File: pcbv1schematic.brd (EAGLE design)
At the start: 275.6 x 183.8 mm, 24 parts, among them IC1 L298, IC2 7805T

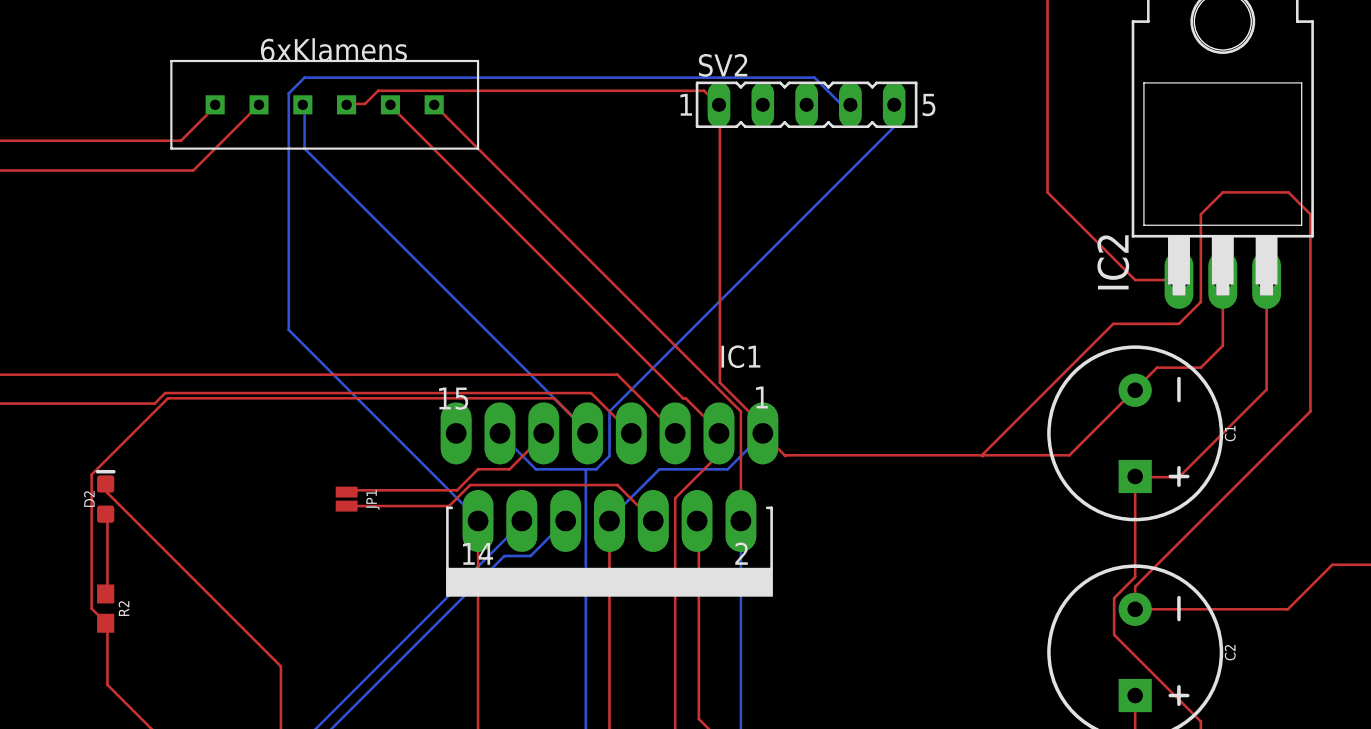
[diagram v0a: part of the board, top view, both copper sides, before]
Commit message: Fixes Label Name
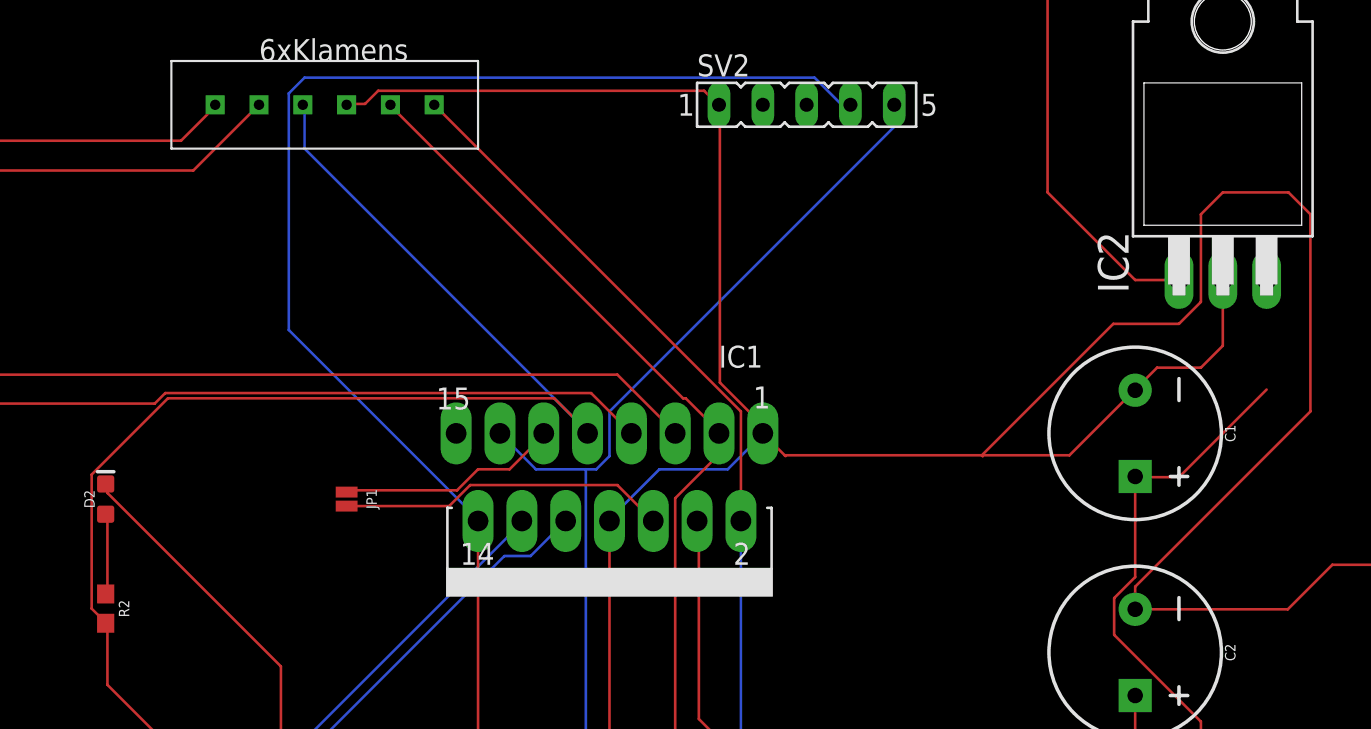
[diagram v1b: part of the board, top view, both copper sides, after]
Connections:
- net N$5 renamed 5V
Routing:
- net 5V: track 211.8 -> 205.0 mm
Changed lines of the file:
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@@
 <drawing>
 <settings>
-<setting alwaysvectorfont="yes"/>
+<setting alwaysvectorfont="no"/>
 <setting verticaltext="up"/>
 </settings>
@@
 <wire x1="43.1292" y1="39.3192" x2="43.18" y2="39.37" width="0.1524" layer="1"/>
 </signal>
-<signal name="N$5">
-<wire x1="125.73" y1="60.96" x2="128.27" y2="60.96" width="0.1524" layer="1"/>
-<wire x1="128.27" y1="60.96" x2="133.35" y2="66.04" width="0.1524" layer="1"/>
-<contactref element="IC2" pad="3"/>
-<contactref element="R2" pad="2"/>
-<contactref element="C1" pad="+"/>
-<contactref element="IC1" pad="9"/>
-<contactref element="U$3" pad="P$3"/>
-<contactref element="U$4" pad="P$3"/>
-<wire x1="125.73" y1="61.1124" x2="125.73" y2="61" width="0.1524" layer="16"/>
-<wire x1="65.2272" y1="53.34" x2="65.9892" y2="52.578" width="0.1524" layer="1"/>
-<wire x1="65.2272" y1="61.1124" x2="65.2272" y2="53.34" width="0.1524" layer="1"/>
-<wire x1="69.6468" y1="65.532" x2="65.2272" y2="61.1124" width="0.1524" layer="1"/>
-<wire x1="92.0496" y1="65.532" x2="69.6468" y2="65.532" width="0.1524" layer="1"/>
-<wire x1="94.0308" y1="63.5508" x2="92.0496" y2="65.532" width="0.1524" layer="1"/>
-<wire x1="65.9892" y1="52.578" x2="66.04" y2="52.49" width="0.1524" layer="1"/>
-<wire x1="94.0308" y1="63.5508" x2="93.98" y2="63.5" width="0.1524" layer="1"/>
-<wire x1="77.4192" y1="37.6428" x2="77.4192" y2="16.6116" width="0.1524" layer="1"/>
-<wire x1="66.1416" y1="48.9204" x2="77.4192" y2="37.6428" width="0.1524" layer="1"/>
-<wire x1="66.1416" y1="52.4256" x2="66.1416" y2="48.9204" width="0.1524" layer="1"/>
-<wire x1="77.4192" y1="16.6116" x2="77.47" y2="16.51" width="0.1524" layer="1"/>
-<wire x1="66.1416" y1="52.4256" x2="66.04" y2="52.49" width="0.1524" layer="1"/>
-<wire x1="77.5716" y1="80.01" x2="77.5716" y2="82.4484" width="0.1524" layer="16"/>
-<wire x1="94.0308" y1="63.5508" x2="77.5716" y2="80.01" width="0.1524" layer="16"/>
-<wire x1="77.5716" y1="82.4484" x2="77.47" y2="82.55" width="0.1524" layer="16"/>
-<wire x1="94.0308" y1="63.5508" x2="93.98" y2="63.5" width="0.1524" layer="16"/>
-<wire x1="125.73" y1="60.96" x2="125.73" y2="61" width="0.1524" layer="16"/>
-<wire x1="94.0308" y1="63.3984" x2="93.98" y2="63.5" width="0.1524" layer="1"/>
-<wire x1="133.35" y1="66.04" x2="133.35" y2="72.39" width="0.1524" layer="1"/>
-<wire x1="125.73" y1="55.1688" x2="125.73" y2="60.96" width="0.1524" layer="1"/>
-<wire x1="124.5108" y1="53.9496" x2="125.73" y2="55.1688" width="0.1524" layer="1"/>
-<wire x1="124.5108" y1="51.816" x2="124.5108" y2="53.9496" width="0.1524" layer="1"/>
-<wire x1="129.54" y1="46.7868" x2="124.5108" y2="51.816" width="0.1524" layer="1"/>
-<wire x1="129.54" y1="36.1188" x2="129.54" y2="46.7868" width="0.1524" layer="1"/>
-<wire x1="109.1184" y1="15.6972" x2="129.54" y2="36.1188" width="0.1524" layer="1"/>
-<wire x1="78.3336" y1="15.6972" x2="109.1184" y2="15.6972" width="0.1524" layer="1"/>
-<wire x1="77.5716" y1="16.4592" x2="78.3336" y2="15.6972" width="0.1524" layer="1"/>
-<wire x1="125.73" y1="60.96" x2="125.73" y2="61" width="0.1524" layer="1"/>
-<wire x1="77.5716" y1="16.4592" x2="77.47" y2="16.51" width="0.1524" layer="1"/>
-</signal>
 <signal name="N$7">
 <wire x1="116.84" y1="62.23" x2="124.46" y2="69.85" width="0.1524" layer="1"/>
@@
 <wire x1="137.16" y1="55.88" x2="143.51" y2="55.88" width="0.1524" layer="1"/>
 </signal>
+<signal name="5V">
+<contactref element="U$3" pad="P$3"/>
+<contactref element="IC2" pad="3"/>
+<contactref element="R2" pad="2"/>
+<contactref element="C1" pad="+"/>
+<wire x1="125.73" y1="61.1124" x2="125.73" y2="61" width="0.1524" layer="16"/>
+<wire x1="125.73" y1="60.96" x2="125.73" y2="61" width="0.1524" layer="16"/>
+<contactref element="IC1" pad="9"/>
+<wire x1="65.2272" y1="53.34" x2="65.9892" y2="52.578" width="0.1524" layer="1"/>
+<wire x1="65.2272" y1="61.1124" x2="65.2272" y2="53.34" width="0.1524" layer="1"/>
+<wire x1="69.6468" y1="65.532" x2="65.2272" y2="61.1124" width="0.1524" layer="1"/>
+<wire x1="92.0496" y1="65.532" x2="69.6468" y2="65.532" width="0.1524" layer="1"/>
+<wire x1="94.0308" y1="63.5508" x2="92.0496" y2="65.532" width="0.1524" layer="1"/>
+<wire x1="94.0308" y1="63.5508" x2="93.98" y2="63.5" width="0.1524" layer="1"/>
+<wire x1="77.5716" y1="80.01" x2="77.5716" y2="82.4484" width="0.1524" layer="16"/>
+<wire x1="94.0308" y1="63.5508" x2="77.5716" y2="80.01" width="0.1524" layer="16"/>
+<wire x1="94.0308" y1="63.5508" x2="93.98" y2="63.5" width="0.1524" layer="16"/>
+<wire x1="94.0308" y1="63.3984" x2="93.98" y2="63.5" width="0.1524" layer="1"/>
+<wire x1="125.73" y1="60.96" x2="128.27" y2="60.96" width="0.1524" layer="1"/>
+<wire x1="128.27" y1="60.96" x2="133.35" y2="66.04" width="0.1524" layer="1"/>
+<contactref element="U$4" pad="P$3"/>
+<wire x1="77.4192" y1="37.6428" x2="77.4192" y2="16.6116" width="0.1524" layer="1"/>
+<wire x1="66.1416" y1="48.9204" x2="77.4192" y2="37.6428" width="0.1524" layer="1"/>
+<wire x1="66.1416" y1="52.4256" x2="66.1416" y2="48.9204" width="0.1524" layer="1"/>
+<wire x1="77.4192" y1="16.6116" x2="77.47" y2="16.51" width="0.1524" layer="1"/>
+<wire x1="125.73" y1="55.1688" x2="125.73" y2="60.96" width="0.1524" layer="1"/>
+<wire x1="124.5108" y1="53.9496" x2="125.73" y2="55.1688" width="0.1524" layer="1"/>
+<wire x1="124.5108" y1="51.816" x2="124.5108" y2="53.9496" width="0.1524" layer="1"/>
+<wire x1="129.54" y1="46.7868" x2="124.5108" y2="51.816" width="0.1524" layer="1"/>
+<wire x1="129.54" y1="36.1188" x2="129.54" y2="46.7868" width="0.1524" layer="1"/>
+<wire x1="109.1184" y1="15.6972" x2="129.54" y2="36.1188" width="0.1524" layer="1"/>
+<wire x1="78.3336" y1="15.6972" x2="109.1184" y2="15.6972" width="0.1524" layer="1"/>
+<wire x1="77.5716" y1="16.4592" x2="78.3336" y2="15.6972" width="0.1524" layer="1"/>
+<wire x1="77.5716" y1="16.4592" x2="77.47" y2="16.51" width="0.1524" layer="1"/>
+<wire x1="133.35" y1="66.04" x2="133.35" y2="72.39" width="0" layer="19" extent="1-1"/>
+<wire x1="66.04" y1="52.49" x2="66.1416" y2="52.4256" width="0" layer="19" extent="1-1"/>
+<wire x1="65.9892" y1="52.578" x2="66.04" y2="52.49" width="0" layer="19" extent="1-1"/>
+<wire x1="77.47" y1="82.55" x2="77.5716" y2="82.4484" width="0" layer="19" extent="16-16"/>
+<wire x1="125.73" y1="61.1124" x2="133.35" y2="66.04" width="0" layer="19" extent="1-16"/>
+</signal>
 </signals>
